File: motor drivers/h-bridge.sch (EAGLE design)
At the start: 5 parts, among them IC1 L298

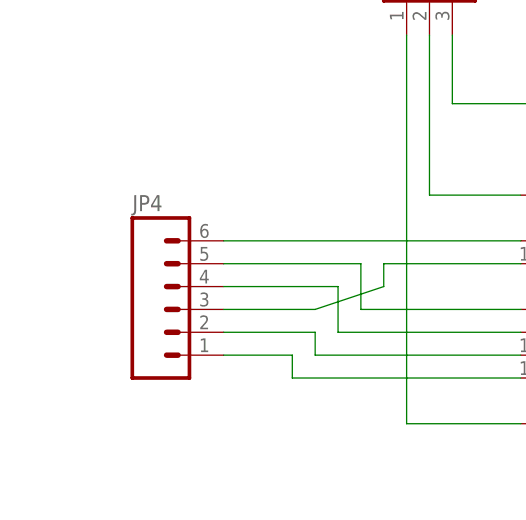
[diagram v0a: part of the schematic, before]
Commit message: fixed iv-18 boardf
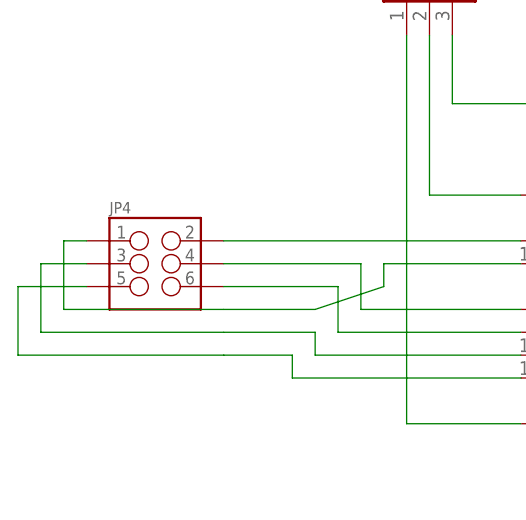
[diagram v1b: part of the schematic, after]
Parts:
- JP4: device iStivi - Header-Connector:M06SIP -> iStivi - Header-Connector:M03X22X3_SILK_SM
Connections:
- net N$10: now also JP4.6; no longer JP4.4
- net N$11: now also JP4.1; no longer JP4.3
- net N$12: now also JP4.3; no longer JP4.2
- net N$13: now also JP4.5; no longer JP4.1
- net N$8: now also JP4.2; no longer JP4.6
- net N$9: now also JP4.4; no longer JP4.5
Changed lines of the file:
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@@
 <grid distance="0.1" unitdist="inch" unit="inch" style="lines" multiple="1" display="no" altdistance="0.01" altunitdist="inch" altunit="inch"/>
 <layers>
-<layer number="1" name="Top" color="4" fill="1" visible="no" active="no"/>
-<layer number="16" name="Bottom" color="1" fill="1" visible="no" active="no"/>
-<layer number="17" name="Pads" color="2" fill="1" visible="no" active="no"/>
-<layer number="18" name="Vias" color="2" fill="1" visible="no" active="no"/>
-<layer number="19" name="Unrouted" color="6" fill="1" visible="no" active="no"/>
-<layer number="20" name="Dimension" color="15" fill="1" visible="no" active="no"/>
-<layer number="21" name="tPlace" color="7" fill="1" visible="no" active="no"/>
-<layer number="22" name="bPlace" color="7" fill="1" visible="no" active="no"/>
-<layer number="23" name="tOrigins" color="15" fill="1" visible="no" active="no"/>
-<layer number="24" name="bOrigins" color="15" fill="1" visible="no" active="no"/>
-<layer number="25" name="tNames" color="7" fill="1" visible="no" active="no"/>
-<layer number="26" name="bNames" color="7" fill="1" visible="no" active="no"/>
-<layer number="27" name="tValues" color="7" fill="1" visible="no" active="no"/>
-<layer number="28" name="bValues" color="7" fill="1" visible="no" active="no"/>
+<layer number="1" name="Top" color="4" fill="1" visible="yes" active="no"/>
+<layer number="16" name="Bottom" color="1" fill="1" visible="yes" active="no"/>
+<layer number="17" name="Pads" color="2" fill="1" visible="yes" active="no"/>
+<layer number="18" name="Vias" color="2" fill="1" visible="yes" active="no"/>
+<layer number="19" name="Unrouted" color="6" fill="1" visible="yes" active="no"/>
+<layer number="20" name="Dimension" color="15" fill="1" visible="yes" active="no"/>
+<layer number="21" name="tPlace" color="7" fill="1" visible="yes" active="no"/>
+<layer number="22" name="bPlace" color="7" fill="1" visible="yes" active="no"/>
+<layer number="23" name="tOrigins" color="15" fill="1" visible="yes" active="no"/>
+<layer number="24" name="bOrigins" color="15" fill="1" visible="yes" active="no"/>
+<layer number="25" name="tNames" color="7" fill="1" visible="yes" active="no"/>
+<layer number="26" name="bNames" color="7" fill="1" visible="yes" active="no"/>
+<layer number="27" name="tValues" color="7" fill="1" visible="yes" active="no"/>
+<layer number="28" name="bValues" color="7" fill="1" visible="yes" active="no"/>
 <layer number="29" name="tStop" color="7" fill="3" visible="no" active="no"/>
 <layer number="30" name="bStop" color="7" fill="6" visible="no" active="no"/>
@@
 <layer number="35" name="tGlue" color="7" fill="4" visible="no" active="no"/>
 <layer number="36" name="bGlue" color="7" fill="5" visible="no" active="no"/>
-<layer number="37" name="tTest" color="7" fill="1" visible="no" active="no"/>
-<layer number="38" name="bTest" color="7" fill="1" visible="no" active="no"/>
+<layer number="37" name="tTest" color="7" fill="1" visible="yes" active="no"/>
+<layer number="38" name="bTest" color="7" fill="1" visible="yes" active="no"/>
 <layer number="39" name="tKeepout" color="4" fill="11" visible="no" active="no"/>
 <layer number="40" name="bKeepout" color="1" fill="11" visible="no" active="no"/>
@@
 <layer number="44" name="Drills" color="7" fill="1" visible="no" active="no"/>
 <layer number="45" name="Holes" color="7" fill="1" visible="no" active="no"/>
-<layer number="46" name="Milling" color="3" fill="1" visible="no" active="no"/>
-<layer number="47" name="Measures" color="7" fill="1" visible="no" active="no"/>
-<layer number="48" name="Document" color="7" fill="1" visible="no" active="no"/>
-<layer number="49" name="Reference" color="7" fill="1" visible="no" active="no"/>
-<layer number="50" name="dxf" color="7" fill="1" visible="no" active="no"/>
-<layer number="51" name="tDocu" color="7" fill="1" visible="no" active="no"/>
-<layer number="52" name="bDocu" color="7" fill="1" visible="no" active="no"/>
-<layer number="53" name="tGND_GNDA" color="7" fill="9" visible="no" active="no"/>
-<layer number="54" name="bGND_GNDA" color="1" fill="9" visible="no" active="no"/>
-<layer number="56" name="wert" color="7" fill="1" visible="no" active="no"/>
+<layer number="46" name="Milling" color="3" fill="1" visible="yes" active="no"/>
+<layer number="47" name="Measures" color="7" fill="1" visible="yes" active="no"/>
+<layer number="48" name="Document" color="7" fill="1" visible="yes" active="no"/>
+<layer number="49" name="Reference" color="7" fill="1" visible="yes" active="no"/>
+<layer number="50" name="dxf" color="7" fill="1" visible="yes" active="no"/>
+<layer number="51" name="tDocu" color="7" fill="1" visible="yes" active="no"/>
+<layer number="52" name="bDocu" color="7" fill="1" visible="yes" active="no"/>
+<layer number="53" name="tGND_GNDA" color="7" fill="9" visible="yes" active="no"/>
+<layer number="54" name="bGND_GNDA" color="1" fill="9" visible="yes" active="no"/>
+<layer number="56" name="wert" color="7" fill="1" visible="yes" active="no"/>
 <layer number="91" name="Nets" color="2" fill="1" visible="yes" active="yes"/>
 <layer number="92" name="Busses" color="1" fill="1" visible="yes" active="yes"/>
@@
 <part name="JP2" library="iStivi - Header-Connector" deviceset="M02" device="3.5MM"/>
 <part name="JP3" library="iStivi - Header-Connector" deviceset="M03" device="SCREW"/>
-<part name="JP4" library="iStivi - Header-Connector" deviceset="M06" device="SIP"/>
+<part name="JP4" library="iStivi - Header-Connector" deviceset="M03X2" device="2X3_SILK_SM"/>
 </parts>
 <sheets>
@@
 <instance part="JP2" gate="G$1" x="114.3" y="45.72" rot="R180"/>
 <instance part="JP3" gate="G$1" x="38.1" y="96.52" rot="R270"/>
-<instance part="JP4" gate="G$1" x="10.16" y="58.42"/>
+<instance part="JP4" gate="G$1" x="7.62" y="63.5"/>
 </instances>
 <busses>
@@
 <segment>
 <pinref part="IC1" gate="L298" pin="ENABLE_A"/>
-<pinref part="JP4" gate="G$1" pin="6"/>
 <wire x1="48.26" y1="66.04" x2="15.24" y2="66.04" width="0.1524" layer="91"/>
+<pinref part="JP4" gate="G$1" pin="2"/>
 </segment>
 </net>
@@
 <wire x1="48.26" y1="58.42" x2="30.48" y2="58.42" width="0.1524" layer="91"/>
 <wire x1="30.48" y1="58.42" x2="30.48" y2="63.5" width="0.1524" layer="91"/>
-<pinref part="JP4" gate="G$1" pin="5"/>
 <wire x1="30.48" y1="63.5" x2="15.24" y2="63.5" width="0.1524" layer="91"/>
+<pinref part="JP4" gate="G$1" pin="4"/>
 </segment>
 </net>
@@
 <wire x1="48.26" y1="55.88" x2="27.94" y2="55.88" width="0.1524" layer="91"/>
 <wire x1="27.94" y1="55.88" x2="27.94" y2="60.96" width="0.1524" layer="91"/>
-<pinref part="JP4" gate="G$1" pin="4"/>
 <wire x1="27.94" y1="60.96" x2="15.24" y2="60.96" width="0.1524" layer="91"/>
+<pinref part="JP4" gate="G$1" pin="6"/>
 </segment>
 </net>
@@
 <wire x1="48.26" y1="63.5" x2="33.02" y2="63.5" width="0.1524" layer="91"/>
 <wire x1="33.02" y1="63.5" x2="33.02" y2="60.96" width="0.1524" layer="91"/>
-<pinref part="JP4" gate="G$1" pin="3"/>
 <wire x1="33.02" y1="60.96" x2="25.4" y2="58.42" width="0.1524" layer="91"/>
 <wire x1="25.4" y1="58.42" x2="15.24" y2="58.42" width="0.1524" layer="91"/>
+<wire x1="15.24" y1="58.42" x2="-2.54" y2="58.42" width="0.1524" layer="91"/>
+<wire x1="-2.54" y1="58.42" x2="-2.54" y2="66.04" width="0.1524" layer="91"/>
+<pinref part="JP4" gate="G$1" pin="1"/>
+<wire x1="-2.54" y1="66.04" x2="0" y2="66.04" width="0.1524" layer="91"/>
 </segment>
 </net>
@@
 <wire x1="48.26" y1="53.34" x2="25.4" y2="53.34" width="0.1524" layer="91"/>
 <wire x1="25.4" y1="53.34" x2="25.4" y2="55.88" width="0.1524" layer="91"/>
-<pinref part="JP4" gate="G$1" pin="2"/>
 <wire x1="25.4" y1="55.88" x2="15.24" y2="55.88" width="0.1524" layer="91"/>
+<wire x1="15.24" y1="55.88" x2="-5.08" y2="55.88" width="0.1524" layer="91"/>
+<wire x1="-5.08" y1="55.88" x2="-5.08" y2="63.5" width="0.1524" layer="91"/>
+<pinref part="JP4" gate="G$1" pin="3"/>
+<wire x1="-5.08" y1="63.5" x2="0" y2="63.5" width="0.1524" layer="91"/>
 </segment>
 </net>
@@
 <wire x1="48.26" y1="50.8" x2="22.86" y2="50.8" width="0.1524" layer="91"/>
 <wire x1="22.86" y1="50.8" x2="22.86" y2="53.34" width="0.1524" layer="91"/>
-<pinref part="JP4" gate="G$1" pin="1"/>
 <wire x1="22.86" y1="53.34" x2="15.24" y2="53.34" width="0.1524" layer="91"/>
-</segment>
-</net>
+<wire x1="15.24" y1="53.34" x2="-7.62" y2="53.34" width="0.1524" layer="91"/>
+<wire x1="-7.62" y1="53.34" x2="-7.62" y2="60.96" width="0.1524" layer="91"/>
+<pinref part="JP4" gate="G$1" pin="5"/>
+<wire x1="-7.62" y1="60.96" x2="0" y2="60.96" width="0.1524" layer="91"/>
+</segment>
+</net>

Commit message: finished routing h-bridge board
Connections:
- net N$1 renamed A_OUT1
- net N$10 renamed A_2
- net N$11 renamed B_EN
- net N$12 renamed B_1
- net N$13 renamed B_2
- net N$2 renamed A_OUT2
- net N$3 renamed B_OUT1
- net N$4 renamed B_OUT2
- net N$5 renamed GND
- net N$6 renamed VS
- net N$7 renamed VCC
- net N$8 renamed A_EN
- net N$9 renamed A_1
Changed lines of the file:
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@@
 <grid distance="0.1" unitdist="inch" unit="inch" style="lines" multiple="1" display="no" altdistance="0.01" altunitdist="inch" altunit="inch"/>
 <layers>
-<layer number="1" name="Top" color="4" fill="1" visible="yes" active="no"/>
-<layer number="16" name="Bottom" color="1" fill="1" visible="yes" active="no"/>
-<layer number="17" name="Pads" color="2" fill="1" visible="yes" active="no"/>
-<layer number="18" name="Vias" color="2" fill="1" visible="yes" active="no"/>
-<layer number="19" name="Unrouted" color="6" fill="1" visible="yes" active="no"/>
-<layer number="20" name="Dimension" color="15" fill="1" visible="yes" active="no"/>
-<layer number="21" name="tPlace" color="7" fill="1" visible="yes" active="no"/>
-<layer number="22" name="bPlace" color="7" fill="1" visible="yes" active="no"/>
-<layer number="23" name="tOrigins" color="15" fill="1" visible="yes" active="no"/>
-<layer number="24" name="bOrigins" color="15" fill="1" visible="yes" active="no"/>
-<layer number="25" name="tNames" color="7" fill="1" visible="yes" active="no"/>
-<layer number="26" name="bNames" color="7" fill="1" visible="yes" active="no"/>
-<layer number="27" name="tValues" color="7" fill="1" visible="yes" active="no"/>
-<layer number="28" name="bValues" color="7" fill="1" visible="yes" active="no"/>
+<layer number="1" name="Top" color="4" fill="1" visible="no" active="no"/>
+<layer number="16" name="Bottom" color="1" fill="1" visible="no" active="no"/>
+<layer number="17" name="Pads" color="2" fill="1" visible="no" active="no"/>
+<layer number="18" name="Vias" color="2" fill="1" visible="no" active="no"/>
+<layer number="19" name="Unrouted" color="6" fill="1" visible="no" active="no"/>
+<layer number="20" name="Dimension" color="15" fill="1" visible="no" active="no"/>
+<layer number="21" name="tPlace" color="7" fill="1" visible="no" active="no"/>
+<layer number="22" name="bPlace" color="7" fill="1" visible="no" active="no"/>
+<layer number="23" name="tOrigins" color="15" fill="1" visible="no" active="no"/>
+<layer number="24" name="bOrigins" color="15" fill="1" visible="no" active="no"/>
+<layer number="25" name="tNames" color="7" fill="1" visible="no" active="no"/>
+<layer number="26" name="bNames" color="7" fill="1" visible="no" active="no"/>
+<layer number="27" name="tValues" color="7" fill="1" visible="no" active="no"/>
+<layer number="28" name="bValues" color="7" fill="1" visible="no" active="no"/>
 <layer number="29" name="tStop" color="7" fill="3" visible="no" active="no"/>
 <layer number="30" name="bStop" color="7" fill="6" visible="no" active="no"/>
@@
 <layer number="35" name="tGlue" color="7" fill="4" visible="no" active="no"/>
 <layer number="36" name="bGlue" color="7" fill="5" visible="no" active="no"/>
-<layer number="37" name="tTest" color="7" fill="1" visible="yes" active="no"/>
-<layer number="38" name="bTest" color="7" fill="1" visible="yes" active="no"/>
+<layer number="37" name="tTest" color="7" fill="1" visible="no" active="no"/>
+<layer number="38" name="bTest" color="7" fill="1" visible="no" active="no"/>
 <layer number="39" name="tKeepout" color="4" fill="11" visible="no" active="no"/>
 <layer number="40" name="bKeepout" color="1" fill="11" visible="no" active="no"/>
@@
 <layer number="44" name="Drills" color="7" fill="1" visible="no" active="no"/>
 <layer number="45" name="Holes" color="7" fill="1" visible="no" active="no"/>
-<layer number="46" name="Milling" color="3" fill="1" visible="yes" active="no"/>
-<layer number="47" name="Measures" color="7" fill="1" visible="yes" active="no"/>
-<layer number="48" name="Document" color="7" fill="1" visible="yes" active="no"/>
-<layer number="49" name="Reference" color="7" fill="1" visible="yes" active="no"/>
-<layer number="50" name="dxf" color="7" fill="1" visible="yes" active="no"/>
-<layer number="51" name="tDocu" color="7" fill="1" visible="yes" active="no"/>
-<layer number="52" name="bDocu" color="7" fill="1" visible="yes" active="no"/>
-<layer number="53" name="tGND_GNDA" color="7" fill="9" visible="yes" active="no"/>
-<layer number="54" name="bGND_GNDA" color="1" fill="9" visible="yes" active="no"/>
-<layer number="56" name="wert" color="7" fill="1" visible="yes" active="no"/>
+<layer number="46" name="Milling" color="3" fill="1" visible="no" active="no"/>
+<layer number="47" name="Measures" color="7" fill="1" visible="no" active="no"/>
+<layer number="48" name="Document" color="7" fill="1" visible="no" active="no"/>
+<layer number="49" name="Reference" color="7" fill="1" visible="no" active="no"/>
+<layer number="50" name="dxf" color="7" fill="1" visible="no" active="no"/>
+<layer number="51" name="tDocu" color="7" fill="1" visible="no" active="no"/>
+<layer number="52" name="bDocu" color="7" fill="1" visible="no" active="no"/>
+<layer number="53" name="tGND_GNDA" color="7" fill="9" visible="no" active="no"/>
+<layer number="54" name="bGND_GNDA" color="1" fill="9" visible="no" active="no"/>
+<layer number="56" name="wert" color="7" fill="1" visible="no" active="no"/>
 <layer number="91" name="Nets" color="2" fill="1" visible="yes" active="yes"/>
 <layer number="92" name="Busses" color="1" fill="1" visible="yes" active="yes"/>
@@
 </busses>
 <nets>
-<net name="N$1" class="0">
+<net name="A_OUT1" class="0">
 <segment>
 <pinref part="IC1" gate="L298" pin="OUT1"/>
@@
 </segment>
 </net>
-<net name="N$2" class="0">
+<net name="A_OUT2" class="0">
 <segment>
 <pinref part="JP1" gate="G$1" pin="2"/>
@@
 </segment>
 </net>
-<net name="N$3" class="0">
+<net name="B_OUT1" class="0">
 <segment>
 <pinref part="JP2" gate="G$1" pin="1"/>
@@
 </segment>
 </net>
-<net name="N$4" class="0">
+<net name="B_OUT2" class="0">
 <segment>
 <pinref part="JP2" gate="G$1" pin="2"/>
@@
 </segment>
 </net>
-<net name="N$5" class="0">
+<net name="GND" class="0">
 <segment>
 <pinref part="IC1" gate="L298" pin="GND"/>
@@
 </segment>
 </net>
-<net name="N$6" class="0">
+<net name="VS" class="0">
 <segment>
 <pinref part="IC1" gate="L298" pin="VS"/>
@@
 </segment>
 </net>
-<net name="N$7" class="0">
+<net name="VCC" class="0">
 <segment>
 <pinref part="IC1" gate="L298" pin="VCC"/>
@@
 </segment>
 </net>
-<net name="N$8" class="0">
+<net name="A_EN" class="0">
 <segment>
 <pinref part="IC1" gate="L298" pin="ENABLE_A"/>
@@
 </segment>
 </net>
-<net name="N$9" class="0">
+<net name="A_1" class="0">
 <segment>
 <pinref part="IC1" gate="L298" pin="INPUT1"/>
@@
 </segment>
 </net>
-<net name="N$10" class="0">
+<net name="A_2" class="0">
 <segment>
 <pinref part="IC1" gate="L298" pin="INPUT2"/>
@@
 </segment>
 </net>
-<net name="N$11" class="0">
+<net name="B_EN" class="0">
 <segment>
 <pinref part="IC1" gate="L298" pin="ENABLE_B"/>
@@
 </segment>
 </net>
-<net name="N$12" class="0">
+<net name="B_1" class="0">
 <segment>
 <pinref part="IC1" gate="L298" pin="INPUT3"/>
@@
 </segment>
 </net>
-<net name="N$13" class="0">
+<net name="B_2" class="0">
 <segment>
 <pinref part="IC1" gate="L298" pin="INPUT4"/>
